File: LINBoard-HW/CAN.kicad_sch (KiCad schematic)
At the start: 11 parts, among them U6 MCP25625x-x-ML, Y2 16MHz 12pF

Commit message: board layout started
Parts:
- C3, C4, C5: footprint Capacitor_SMD:C_0603_1608Metric -> Capacitor_SMD:C_0402_1005Metric
- R17, R18, R19, R4: footprint Resistor_SMD:R_0603_1608Metric -> Resistor_SMD:R_0402_1005Metric
- Y2: footprint (none) -> Crystal:Crystal_SMD_3225-4Pin_3.2x2.5mm
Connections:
- net at C4.1, U6.20 (OSC2): now also Y2.2; no longer Y2.1
- net at C5.1, U6.21 (OSC1): now also Y2.1; no longer Y2.2
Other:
- moved on the sheet: Y2
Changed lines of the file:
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@@
 			)
 		)
-		(property "Footprint" "Resistor_SMD:R_0603_1608Metric"
+		(property "Footprint" "Resistor_SMD:R_0402_1005Metric"
 			(at 102.87 137.16 0)
 			(effects
@@
 			)
 		)
-		(property "Footprint" "Resistor_SMD:R_0603_1608Metric"
+		(property "Footprint" "Resistor_SMD:R_0402_1005Metric"
 			(at 102.87 118.11 0)
 			(effects
@@
 			)
 		)
-		(property "Footprint" "Capacitor_SMD:C_0603_1608Metric"
+		(property "Footprint" "Capacitor_SMD:C_0402_1005Metric"
 			(at 172.72 105.41 0)
 			(effects
@@
 			)
 		)
-		(property "Footprint" "Capacitor_SMD:C_0603_1608Metric"
+		(property "Footprint" "Capacitor_SMD:C_0402_1005Metric"
 			(at 172.72 113.03 0)
 			(effects
@@
 	(symbol
 		(lib_id "Device:Crystal_Small")
-		(at 151.13 109.22 90)
+		(at 151.13 109.22 270)
 		(unit 1)
 		(exclude_from_sim no)
@@
 					(size 1.27 1.27)
 				)
-				(justify right)
+				(justify left)
 			)
 		)
@@
 					(size 1.27 1.27)
 				)
-				(justify right)
-			)
-		)
-		(property "Footprint" ""
+				(justify left)
+			)
+		)
+		(property "Footprint" "Crystal:Crystal_SMD_3225-4Pin_3.2x2.5mm"
 			(at 151.13 109.22 0)
 			(effects
@@
 			)
 		)
-		(property "Footprint" "Resistor_SMD:R_0603_1608Metric"
+		(property "Footprint" "Resistor_SMD:R_0402_1005Metric"
 			(at 102.87 90.17 0)
 			(effects
@@
 			)
 		)
-		(property "Footprint" "Resistor_SMD:R_0603_1608Metric"
+		(property "Footprint" "Resistor_SMD:R_0402_1005Metric"
 			(at 181.61 76.2 0)
 			(effects
@@
 			)
 		)
-		(property "Footprint" "Capacitor_SMD:C_0603_1608Metric"
+		(property "Footprint" "Capacitor_SMD:C_0402_1005Metric"
 			(at 207.01 46.99 0)
 			(effects

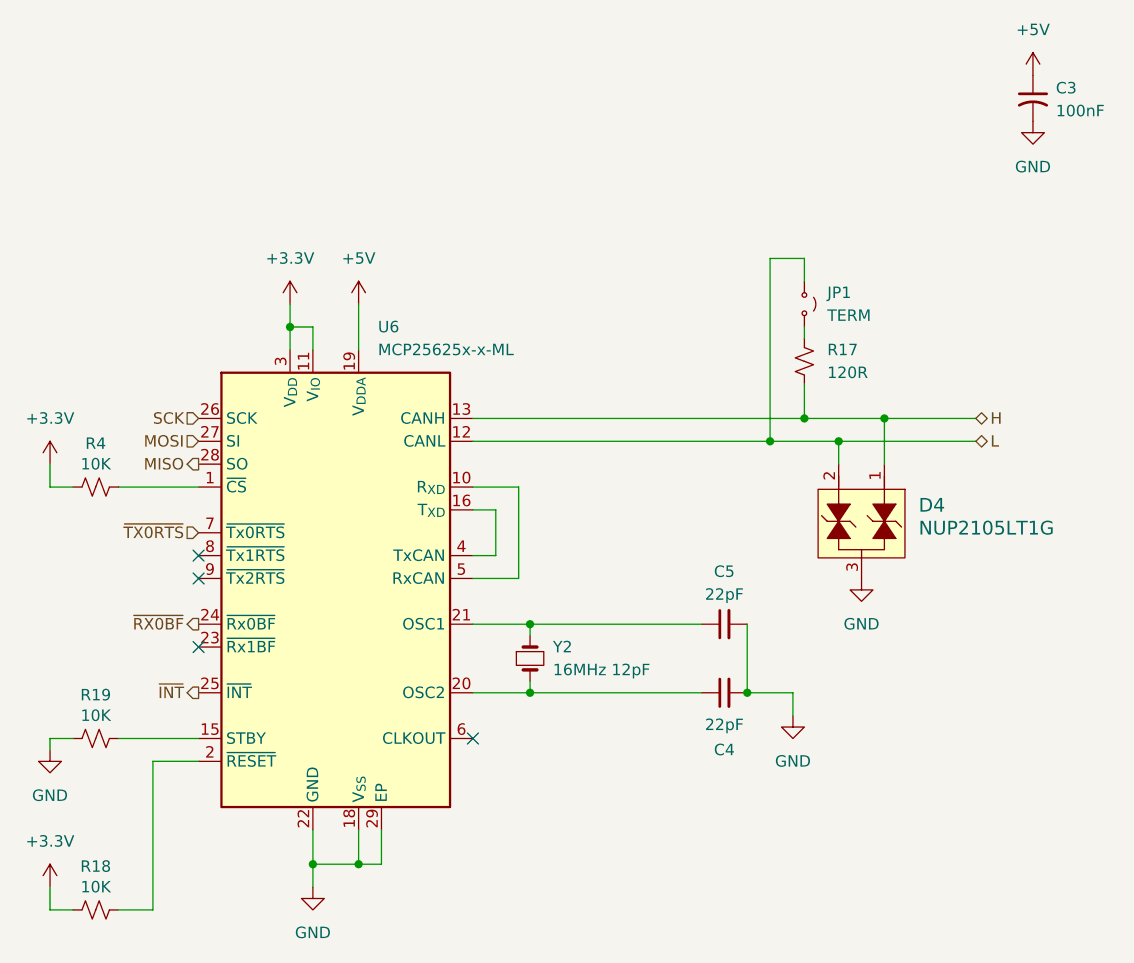
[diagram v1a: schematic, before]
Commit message: change usb
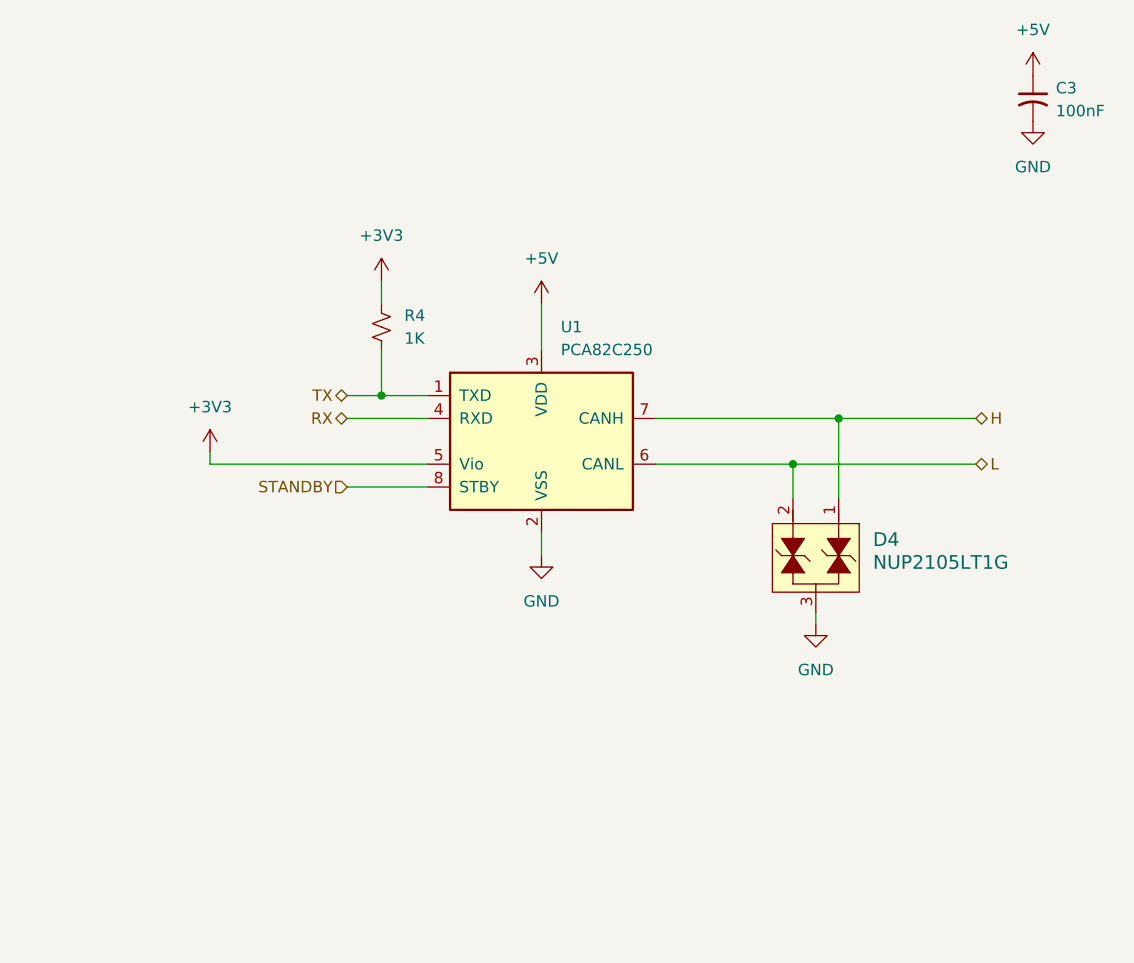
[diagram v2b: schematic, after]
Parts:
- removed C4, C5: 22pF, Capacitor_SMD:C_0402_1005Metric, symbol Device:C_Small
- removed JP1: TERM, Jumper:SolderJumper-2_P1.3mm_Open_RoundedPad1.0x1.5mm, symbol Jumper:Jumper_2_Small_Open
- removed R17: 120R, Resistor_SMD:R_0402_1005Metric, symbol Device:R_Small_US
- removed R18, R19: 10K, Resistor_SMD:R_0402_1005Metric, symbol Device:R_Small_US
- removed U6: MCP25625x-x-ML, Package_DFN_QFN:QFN-28-1EP_6x6mm_P0.65mm_EP4.25x4.25mm, symbol Interface_CAN_LIN:MCP25625x-x-ML
- removed Y2: 16MHz 12pF, Crystal:Crystal_SMD_3225-4Pin_3.2x2.5mm, symbol Device:Crystal_Small
- added U1: PCA82C250, Package_SO:SOIC-8_3.9x4.9mm_P1.27mm, symbol Interface_CAN_LIN:MCP2562-E-SN
- R4: value 10K -> 1K
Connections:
- net +5V: now also U1.3 (VDD)
- net GND: now also U1.2 (VSS)
- net H: now also U1.7 (CANH)
- net L: now also U1.6 (CANL)
- net TX: now reaches R4.2
- net TX: now also U1.1 (TXD)
- net +3.3V renamed +3V3
- net +3V3: now also U1.5 (Vio)
- new net RX: U1.4 (RXD)
- new net STANDBY: U1.8 (STBY)
- no-connect marks 4 -> 0

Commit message: doing some layout
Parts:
- C3: footprint Capacitor_SMD:C_0402_1005Metric -> Capacitor_SMD:C_0805_2012Metric
- R4: footprint Resistor_SMD:R_0402_1005Metric -> Resistor_SMD:R_0805_2012Metric
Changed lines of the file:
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@@
 			)
 		)
-		(property "Footprint" "Resistor_SMD:R_0402_1005Metric"
+		(property "Footprint" "Resistor_SMD:R_0805_2012Metric"
 			(at 134.62 72.39 0)
 			(effects
@@
 			)
 		)
-		(property "Footprint" "Capacitor_SMD:C_0402_1005Metric"
+		(property "Footprint" "Capacitor_SMD:C_0805_2012Metric"
 			(at 207.01 46.99 0)
 			(effects

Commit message: routing first pass complete
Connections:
- net H: now also D4.2; no longer D4.1
- net L: now also D4.1; no longer D4.2
- net +3V3 renamed +3.3V
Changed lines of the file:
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@@
 	)
 	(junction
-		(at 180.34 87.63)
+		(at 180.34 82.55)
+		(diameter 0)
+		(color 0 0 0 0)
+	)
+	(junction
+		(at 185.42 87.63)
 		(diameter 0)
 		(color 0 0 0 0)
@@
 		(color 0 0 0 0)
 	)
-	(junction
-		(at 185.42 82.55)
-		(diameter 0)
-		(color 0 0 0 0)
-	)
 	(wire
 		(pts
@@
 	(wire
 		(pts
+			(xy 185.42 87.63) (xy 185.42 91.44)
+		)
+		(stroke
+			(width 0)
+			(type default)
+		)
+	)
+	(wire
+		(pts
 			(xy 134.62 74.93) (xy 134.62 80.01)
 		)
@@
 	(wire
 		(pts
+			(xy 185.42 87.63) (xy 200.66 87.63)
+		)
+		(stroke
+			(width 0)
+			(type default)
+		)
+	)
+	(wire
+		(pts
 			(xy 130.81 80.01) (xy 134.62 80.01)
 		)
@@
 	(wire
 		(pts
-			(xy 180.34 87.63) (xy 200.66 87.63)
-		)
-		(stroke
-			(width 0)
-			(type default)
-		)
-	)
-	(wire
-		(pts
-			(xy 165.1 87.63) (xy 180.34 87.63)
+			(xy 165.1 87.63) (xy 185.42 87.63)
+		)
+		(stroke
+			(width 0)
+			(type default)
+		)
+	)
+	(wire
+		(pts
+			(xy 180.34 82.55) (xy 180.34 91.44)
 		)
 		(stroke
@@
 	(wire
 		(pts
-			(xy 165.1 82.55) (xy 185.42 82.55)
+			(xy 180.34 82.55) (xy 200.66 82.55)
+		)
+		(stroke
+			(width 0)
+			(type default)
+		)
+	)
+	(wire
+		(pts
+			(xy 165.1 82.55) (xy 180.34 82.55)
 		)
 		(stroke
@@
 	(wire
 		(pts
-			(xy 185.42 82.55) (xy 200.66 82.55)
-		)
-		(stroke
-			(width 0)
-			(type default)
-		)
-	)
-	(wire
-		(pts
-			(xy 185.42 82.55) (xy 185.42 91.44)
-		)
-		(stroke
-			(width 0)
-			(type default)
-		)
-	)
-	(wire
-		(pts
 			(xy 152.4 95.25) (xy 152.4 97.79)
 		)
@@
 		(pts
 			(xy 152.4 69.85) (xy 152.4 74.93)
-		)
-		(stroke
-			(width 0)
-			(type default)
-		)
-	)
-	(wire
-		(pts
-			(xy 180.34 87.63) (xy 180.34 91.44)
 		)
 		(stroke
@@
 			)
 			(justify right)
-		)
-	)
-	(symbol
-		(lib_id "power:+3V3")
-		(at 134.62 67.31 0)
-		(unit 1)
-		(exclude_from_sim no)
-		(in_bom yes)
-		(on_board yes)
-		(dnp no)
-		(fields_autoplaced yes)
-		(property "Reference" "#PWR022"
-			(at 134.62 71.12 0)
-			(effects
-				(font
-					(size 1.27 1.27)
-				)
-				(hide yes)
-			)
-		)
-		(property "Value" "+3V3"
-			(at 134.62 62.23 0)
-			(effects
-				(font
-					(size 1.27 1.27)
-				)
-			)
-		)
-		(property "Footprint" ""
-			(at 134.62 67.31 0)
-			(effects
-				(font
-					(size 1.27 1.27)
-				)
-				(hide yes)
-			)
-		)
-		(property "Datasheet" ""
-			(at 134.62 67.31 0)
-			(effects
-				(font
-					(size 1.27 1.27)
-				)
-				(hide yes)
-			)
-		)
-		(property "Description" "Power symbol creates a global label with name \"+3V3\""
-			(at 134.62 67.31 0)
-			(effects
-				(font
-					(size 1.27 1.27)
-				)
-				(hide yes)
-			)
-		)
-		(pin "1"
-		)
-		(instances
-			(project ""
-				(path "/27863e5d-8a22-474c-850d-36d8970b0f4a/b4409545-53c7-4f50-ab4b-a05376db3f02"
-					(reference "#PWR022")
-					(unit 1)
-				)
-			)
 		)
 	)
@@
 	)
 	(symbol
+		(lib_id "power:+3.3V")
+		(at 115.57 86.36 0)
+		(unit 1)
+		(exclude_from_sim no)
+		(in_bom yes)
+		(on_board yes)
+		(dnp no)
+		(fields_autoplaced yes)
+		(property "Reference" "#PWR023"
+			(at 115.57 90.17 0)
+			(effects
+				(font
+					(size 1.27 1.27)
+				)
+				(hide yes)
+			)
+		)
+		(property "Value" "+3.3V"
+			(at 115.57 81.28 0)
+			(effects
+				(font
+					(size 1.27 1.27)
+				)
+			)
+		)
+		(property "Footprint" ""
+			(at 115.57 86.36 0)
+			(effects
+				(font
+					(size 1.27 1.27)
+				)
+				(hide yes)
+			)
+		)
+		(property "Datasheet" ""
+			(at 115.57 86.36 0)
+			(effects
+				(font
+					(size 1.27 1.27)
+				)
+				(hide yes)
+			)
+		)
+		(property "Description" "Power symbol creates a global label with name \"+3.3V\""
+			(at 115.57 86.36 0)
+			(effects
+				(font
+					(size 1.27 1.27)
+				)
+				(hide yes)
+			)
+		)
+		(pin "1"
+		)
+		(instances
+			(project "LINBoard-HW"
+				(path "/27863e5d-8a22-474c-850d-36d8970b0f4a/b4409545-53c7-4f50-ab4b-a05376db3f02"
+					(reference "#PWR023")
+					(unit 1)
+				)
+			)
+		)
+	)
+	(symbol
 		(lib_id "power:GND")
 		(at 182.88 105.41 0)
@@
 	)
 	(symbol
-		(lib_id "power:+3V3")
-		(at 115.57 86.36 0)
+		(lib_id "power:+3.3V")
+		(at 134.62 67.31 0)
 		(unit 1)
 		(exclude_from_sim no)
@@
 		(dnp no)
 		(fields_autoplaced yes)
-		(property "Reference" "#PWR023"
-			(at 115.57 90.17 0)
-			(effects
-				(font
-					(size 1.27 1.27)
-				)
-				(hide yes)
-			)
-		)
-		(property "Value" "+3V3"
-			(at 115.57 81.28 0)
+		(property "Reference" "#PWR022"
+			(at 134.62 71.12 0)
+			(effects
+				(font
+					(size 1.27 1.27)
+				)
+				(hide yes)
+			)
+		)
+		(property "Value" "+3.3V"
+			(at 134.62 62.23 0)
 			(effects
 				(font
@@
 		)
 		(property "Footprint" ""
-			(at 115.57 86.36 0)
+			(at 134.62 67.31 0)
 			(effects
 				(font
@@
 		)
 		(property "Datasheet" ""
-			(at 115.57 86.36 0)
-			(effects
-				(font
-					(size 1.27 1.27)
-				)
-				(hide yes)
-			)
-		)
-		(property "Description" "Power symbol creates a global label with name \"+3V3\""
-			(at 115.57 86.36 0)
+			(at 134.62 67.31 0)
+			(effects
+				(font
+					(size 1.27 1.27)
+				)
+				(hide yes)
+			)
+		)
+		(property "Description" "Power symbol creates a global label with name \"+3.3V\""
+			(at 134.62 67.31 0)
 			(effects
 				(font
@@
 		)
 		(instances
-			(project "LINBoard-HW"
+			(project ""
 				(path "/27863e5d-8a22-474c-850d-36d8970b0f4a/b4409545-53c7-4f50-ab4b-a05376db3f02"
-					(reference "#PWR023")
+					(reference "#PWR022")
 					(unit 1)
 				)

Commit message: add fab outputs
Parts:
- C3: LCSC Part (none) -> C49678
- D4: LCSC Part (none) -> C2976509
- R4: LCSC Part (none) -> C17513
- U1: LCSC Part (none) -> C7439
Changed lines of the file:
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@@
+			)
+		)
+		(property "LCSC Part" "C17513"
+			(at 134.62 72.39 0)
+			(effects
+				(font
+					(size 1.27 1.27)
+				)
+				(hide yes)
 			)
 		)
@@
 			)
 		)
+		(property "LCSC Part" "C2976509"
+			(at 182.88 99.06 90)
+			(effects
+				(font
+					(size 1.27 1.27)
+				)
+				(hide yes)
+			)
+		)
 		(pin "1"
 		)
@@
 			)
 		)
+		(property "LCSC Part" "C7439"
+			(at 152.4 85.09 0)
+			(effects
+				(font
+					(size 1.27 1.27)
+				)
+				(hide yes)
+			)
+		)
 		(pin "5"
 		)
@@
 			(at 207.01 46.99 0)
 			(effects
+				(font
+					(size 1.27 1.27)
+				)
+				(hide yes)
+			)
+		)
+		(property "LCSC Part" "C49678"
+			(at 207.01 46.99 0)
+			(effects
